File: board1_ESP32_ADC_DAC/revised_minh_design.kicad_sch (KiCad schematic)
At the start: 15 parts, among them J1 Conn_01x03_Male, J2 Conn_01x07_Male, U1 ESP32-DevKit-C, U2 LM7805_TO220, U3 NE5532, U4 CB101

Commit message: -
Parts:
- removed C3: 0.1uF, Capacitor_THT:C_Disc_D6.0mm_W2.5mm_P5.00mm, symbol Device:C
- removed D1: TZX3V6A-TR, Diode_THT:D_DO-35_SOD27_P7.62mm_Horizontal, symbol Device:D_Zener
- removed D2: LED, LED_THT:LED_D3.0mm_Clear, symbol Device:LED
- removed J2: Conn_01x07_Male, Connector_PinSocket_2.54mm:PinSocket_1x07_P2.54mm_Vertical, symbol Connector:Conn_01x07_Male
- removed R1, R2: 10k, Resistor_THT:R_Axial_DIN0309_L9.0mm_D3.2mm_P15.24mm_Horizontal, symbol Device:R
- removed R3: 1K, Resistor_THT:R_Axial_DIN0309_L9.0mm_D3.2mm_P15.24mm_Horizontal, symbol Device:R
- removed R4: 4.7k, Resistor_THT:R_Axial_DIN0309_L9.0mm_D3.2mm_P15.24mm_Horizontal, symbol Device:R
- removed U3: NE5532, Package_DIP:DIP-8_W7.62mm, symbol Amplifier_Operational:NE5532
- removed U4: CB101, Library:CB101, symbol design:CB101
- added C? (x2): 2.2uF, Capacitor_THT:C_Disc_D6.0mm_W2.5mm_P5.00mm, symbol Device:C
- added C?: 1uF, Capacitor_THT:C_Disc_D6.0mm_W2.5mm_P5.00mm, symbol Device:C
- added C?: 1nF, Capacitor_THT:C_Disc_D6.0mm_W2.5mm_P5.00mm, symbol Device:C
- added J?: Conn_01x08_Male, symbol Connector:Conn_01x08_Male
- added R?: 0, symbol Device:R
- added R?: R, symbol Device:R
- added U?: DAC8568IAPW, Package_SO:TSSOP-16-1EP_4.4x5mm_P0.65mm, symbol design:DAC8568IAPW
- added U?: MCP1501-33xSN, Package_SO:SOIC-8_3.9x4.9mm_P1.27mm, symbol Reference_Voltage:MCP1501-33xSN
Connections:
- net +5V: now also C?.1, U?.1 (VDD), U?.3 (~{SHDN})
- net Earth: now also C?.2, C?.2, C?.2, C?.2, U?.14 (GND), U?.2 (GND), U?.4 (GND), U?.5 (GND), U?.6 (GND)
- net +3V3: now reaches U1.20 (3V3)
- net +3V3: now also C?.1, U?.3 (AV_{DD})
- net ~{CS}: now reaches U1.30 (27)
- net ~{CS}: now also U?.2 (~{SYNC})
- net SK: now reaches U1.31 (14)
- net SK: now also U?.16 (SCLK)
- net SO: now reaches U1.34 (13)
- net SO: now also U?.15 (D_{IN})
- net LDAC: now reaches U1.8 (16)
- net LDAC: now also U?.1 (LDAC)
- net ~{CLR}: now reaches U1.9 (17)
- net ~{CLR}: now also U?.9 (~{CLR})
- net DAC_SIG: no longer names the net of U1.28 (25)
- new net: C?.1, R?.2
- new net: R?.2, U?.8 (V_{REF}IN)
- new net +3.3VDAC: C?.1, R?.1, R?.1, U?.7 (OUT), U?.8 (FB)
- new net VoutA: J?.8 (Pin_8), U?.4 (V_{OUT}A)
- new net VoutB: J?.7 (Pin_7), U?.13 (V_{OUT}B)
- new net VoutC: J?.6 (Pin_6), U?.5 (V_{OUT}C)
- new net VoutD: J?.5 (Pin_5), U?.12 (V_{OUT}D)
- new net VoutE: J?.4 (Pin_4), U?.6 (V_{OUT}E)
- new net VoutF: J?.3 (Pin_3), U?.11 (V_{OUT}F)
- new net VoutG: J?.2 (Pin_2), U?.7 (V_{OUT}G)
- new net VoutH: J?.1 (Pin_1), U?.10 (V_{OUT}H)
- no-connect marks 38 -> 28
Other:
- note added: "MOSI"
- note added: "SCLK"
- note removed: "Vout/Vin = 1 + 4.7/10"
- moved on the sheet: C1, C2, J1, U1, U2

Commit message: ADC_DAC
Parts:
- added C11, C4, C5, C6, C7: 0.1uF, Capacitor_SMD:C_0805_2012Metric_Pad1.18x1.45mm_HandSolder, symbol Device:C
- added C3, C8, C9: 10uF, Capacitor_SMD:C_0805_2012Metric_Pad1.18x1.45mm_HandSolder, symbol Device:C
- added J3, J4: Conn_01x08_Male, Connector_PinSocket_2.54mm:PinSocket_1x08_P2.54mm_Vertical, symbol Connector:Conn_01x08_Male
- added R1, R3: 0, Resistor_SMD:R_0805_2012Metric_Pad1.20x1.40mm_HandSolder, symbol Device:R
- added U3: MCP1754S-3302xCB, Package_TO_SOT_SMD:SOT-23, symbol Regulator_Linear:MCP1754S-3302xCB
- added U4: MCP1825S-3.3V, Package_TO_SOT_SMD:SOT-223-3_TabPin2, symbol Regulator_Linear:MCP1825S
- added U6, U7: MCP3464R, Package_SO:TSSOP-20_4.4x6.5mm_P0.65mm, symbol design:MCP3464R
- added X1: ECS-2520MVLC-049-BN-TR, Oscillator:Oscillator_SMD_ECS_2520MV-xxx-xx-4Pin_2.5x2.0mm, symbol Oscillator:ECS-2520MV-xxx-xx
- C1, C2: footprint Capacitor_THT:C_Disc_D6.0mm_W2.5mm_P5.00mm -> Capacitor_SMD:C_0805_2012Metric_Pad1.18x1.45mm_HandSolder
- C10, C12, C13, C14: renamed from C?; footprint Capacitor_THT:C_Disc_D6.0mm_W2.5mm_P5.00mm -> Capacitor_SMD:C_0805_2012Metric_Pad1.18x1.45mm_HandSolder
- J2: renamed from J?; footprint (none) -> Connector_PinSocket_2.54mm:PinSocket_1x08_P2.54mm_Vertical
- R2: renamed from R?; value R -> 50; footprint (none) -> Resistor_SMD:R_0805_2012Metric_Pad1.20x1.40mm_HandSolder
- R4: renamed from R?; footprint (none) -> Resistor_SMD:R_0805_2012Metric_Pad1.20x1.40mm_HandSolder
- gave numbers to parts that had none: 2
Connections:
- net +3.3VDAC: now also U6.4 (REFIN+), U7.4 (REFIN+)
- net +3V3: now also C11.1, C7.1, C9.1, U4.3 (VO), U6.20 (DV_{DD}), U7.20 (DV_{DD}), X1.4 (VDD); no longer U1.20 (3V3)
- net +5V: now also C3.1, C4.1, C5.1, U3.3 (VI), U4.1 (VI)
- net Earth: now also C11.2, C3.2, C5.2, C7.2, C9.2, R1.1, U4.2 (GND), U6.19 (D_{GND}), U7.19 (D_{GND}), X1.2 (GND)
- net SK: now also U6.14 (SCK), U7.14 (SCK)
- net SO: now also U6.16 (SDO), U7.16 (SDO)
- net VoutB: now also J2.1 (Pin_1); no longer J2.7 (Pin_7)
- net VoutC: now also J2.7 (Pin_7); no longer J2.6 (Pin_6)
- net VoutD: now also J2.2 (Pin_2); no longer J2.5 (Pin_5)
- net VoutE: now also J2.6 (Pin_6); no longer J2.4 (Pin_4)
- net VoutG: now also J2.5 (Pin_5); no longer J2.2 (Pin_2)
- net VoutH: now also J2.4 (Pin_4); no longer J2.1 (Pin_1)
- net MDAT: now reaches U1.25 (35)
- net MDAT: now also U6.17 (~{IRQ}/MDAT), U7.17 (~{IRQ}/MDAT)
- net ~{ADC2_CS}: now reaches U1.26 (32)
- net ~{ADC2_CS}: now also U7.13 (~{CS})
- net ~{ADC1_CS}: now reaches U1.27 (33)
- net ~{ADC1_CS}: now also U6.13 (~{CS})
- net SI: now reaches U1.32 (12)
- net SI: now also U6.15 (SDI), U7.15 (SDI)
- net ~{CS} renamed ~{DAC_CS}
- new net: R3.1, X1.3 (OUT)
- new net +3.3VA: C6.1, C8.1, U3.2 (VO), U6.1 (AV_{DD}), U7.1 (AV_{DD})
- new net ADC1_1: J4.1 (Pin_1), U6.5 (CH0)
- new net ADC1_2: J4.2 (Pin_2), U6.6 (CH1)
- new net ADC1_3: J4.3 (Pin_3), U6.7 (CH2)
- new net ADC1_4: J4.4 (Pin_4), U6.8 (CH3)
- new net ADC1_5: J4.5 (Pin_5), U6.9 (CH4)
- new net ADC1_6: J4.6 (Pin_6), U6.10 (CH5)
- new net ADC1_7: J4.7 (Pin_7), U6.11 (CH6)
- new net ADC1_8: J4.8 (Pin_8), U6.12 (CH7)
- new net ADC2_1: J3.1 (Pin_1), U7.5 (CH0)
- new net ADC2_2: J3.2 (Pin_2), U7.6 (CH1)
- new net ADC2_3: J3.3 (Pin_3), U7.7 (CH2)
- new net ADC2_4: J3.4 (Pin_4), U7.8 (CH3)
- new net ADC2_5: J3.5 (Pin_5), U7.9 (CH4)
- new net ADC2_6: J3.6 (Pin_6), U7.10 (CH5)
- new net ADC2_7: J3.7 (Pin_7), U7.11 (CH6)
- new net ADC2_8: J3.8 (Pin_8), U7.12 (CH7)
- new net CLK: R3.2, U6.18 (MLCK), U7.18 (MLCK)
- new net GNDA: C4.2, C6.2, C8.2, R1.2, U3.1 (GND), U6.2 (A_{GND}), U6.3 (REFIN-), U7.2 (A_{GND}), U7.3 (REFIN-)
- no-connect marks 28 -> 26
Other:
- moved on the sheet: C14, J2, R4, U1, U8

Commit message: DAC ground to AGND, new AGND polygon pour
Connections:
- net Earth: no longer U8.14 (GND)
- net GNDA: now also U8.14 (GND)
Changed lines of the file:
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@@
+    (pin "1")
+  )
+  (symbol (lib_id "power:GNDA") (at 220.98 68.58 0) (unit 1)
+    (in_bom yes) (on_board yes)
+    (property "Reference" "#PWR?" (id 0) (at 220.98 74.93 0)
+      (effects (font (size 1.27 1.27)) hide)
+    )
+    (property "Value" "GNDA" (id 1) (at 217.17 69.85 0))
+    (property "Footprint" "" (id 2) (at 220.98 68.58 0)
+      (effects (font (size 1.27 1.27)) hide)
+    )
+    (property "Datasheet" "" (id 3) (at 220.98 68.58 0)
+      (effects (font (size 1.27 1.27)) hide)
+    )
     (pin "1")
   )
@@
     (pin "1")
   )
-  (symbol (lib_id "power:Earth") (at 220.98 68.58 0) (unit 1)
-    (in_bom yes) (on_board yes) (fields_autoplaced)
-    (property "Reference" "#PWR040" (id 0) (at 220.98 74.93 0)
-      (effects (font (size 1.27 1.27)) hide)
-    )
-    (property "Value" "Earth" (id 1) (at 220.98 72.39 0)
-      (effects (font (size 1.27 1.27)) hide)
-    )
-    (property "Footprint" "" (id 2) (at 220.98 68.58 0)
-      (effects (font (size 1.27 1.27)) hide)
-    )
-    (property "Datasheet" "~" (id 3) (at 220.98 68.58 0)
-      (effects (font (size 1.27 1.27)) hide)
-    )
-    (pin "1")
-  )
   (symbol (lib_id "Device:C") (at 87.63 33.02 0) (unit 1)
     (in_bom yes) (on_board yes) (fields_autoplaced)
@@
       (reference "#PWR039") (unit 1) (value "Earth") (footprint "")
     )
-    (path "/ded4a434-8dc3-4ae9-9c86-aa80321c8438"
-      (reference "#PWR040") (unit 1) (value "Earth") (footprint "")
-    )
     (path "/a693dd2a-10f5-49e8-8ed2-7ff749236d48"
       (reference "#PWR041") (unit 1) (value "+3.3V") (footprint "")
@@
       (reference "#PWR047") (unit 1) (value "+3.3V") (footprint "")
     )
+    (path "/1608183c-7910-43a9-a0f7-77336bb08a03"
+      (reference "#PWR?") (unit 1) (value "GNDA") (footprint "")
+    )
     (path "/f1973fc8-15b6-4c53-87c0-78a3b2cf3358"

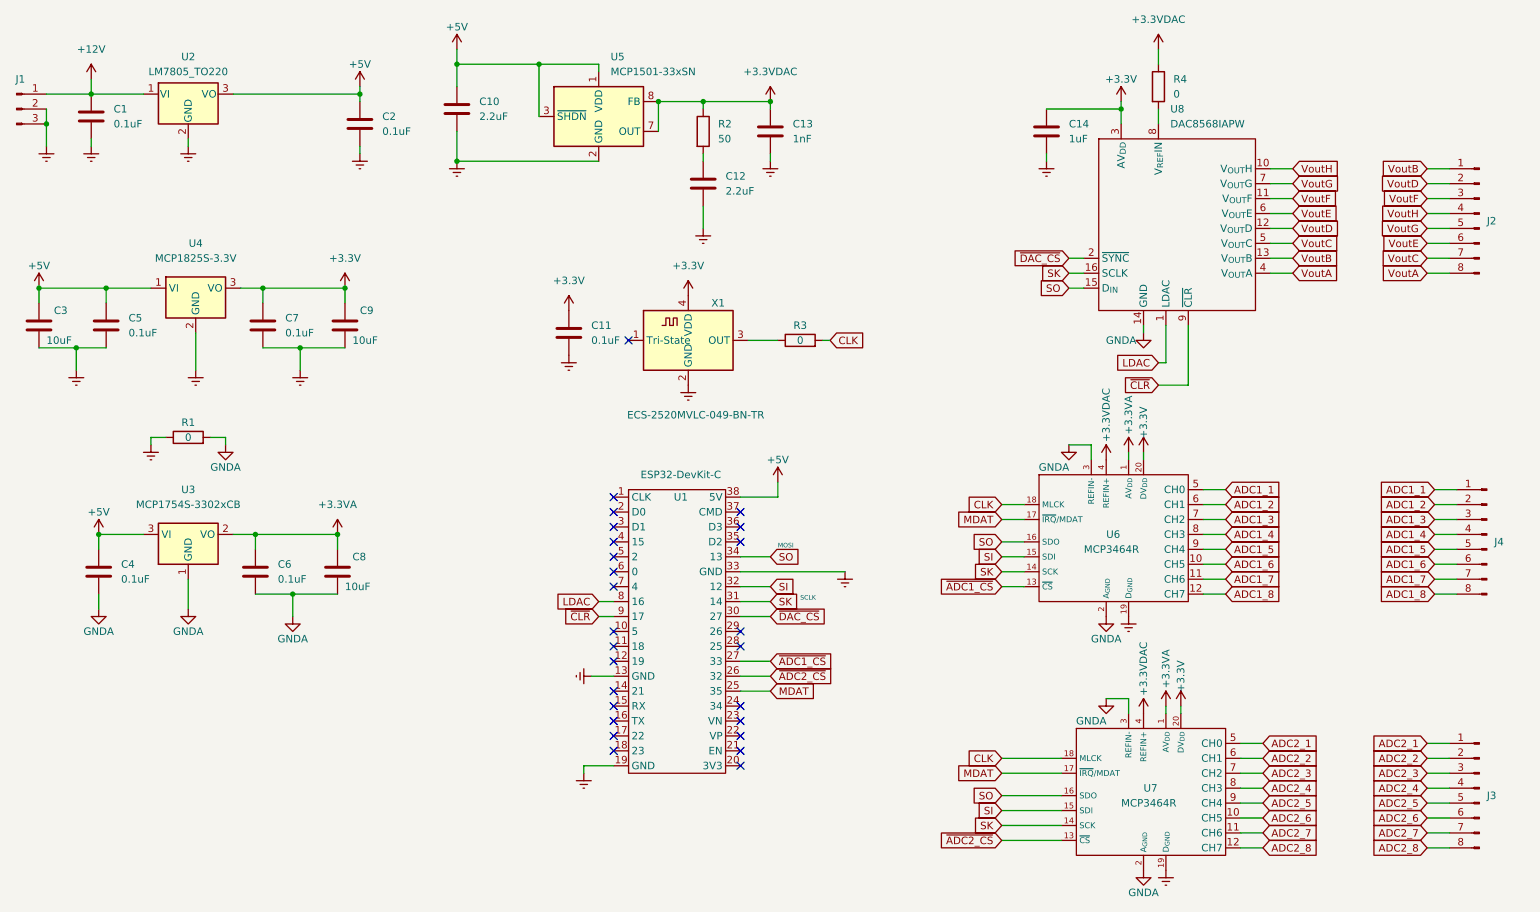
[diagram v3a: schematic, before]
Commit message: Fab ready version with joined ground plane, extra caps for ADCs
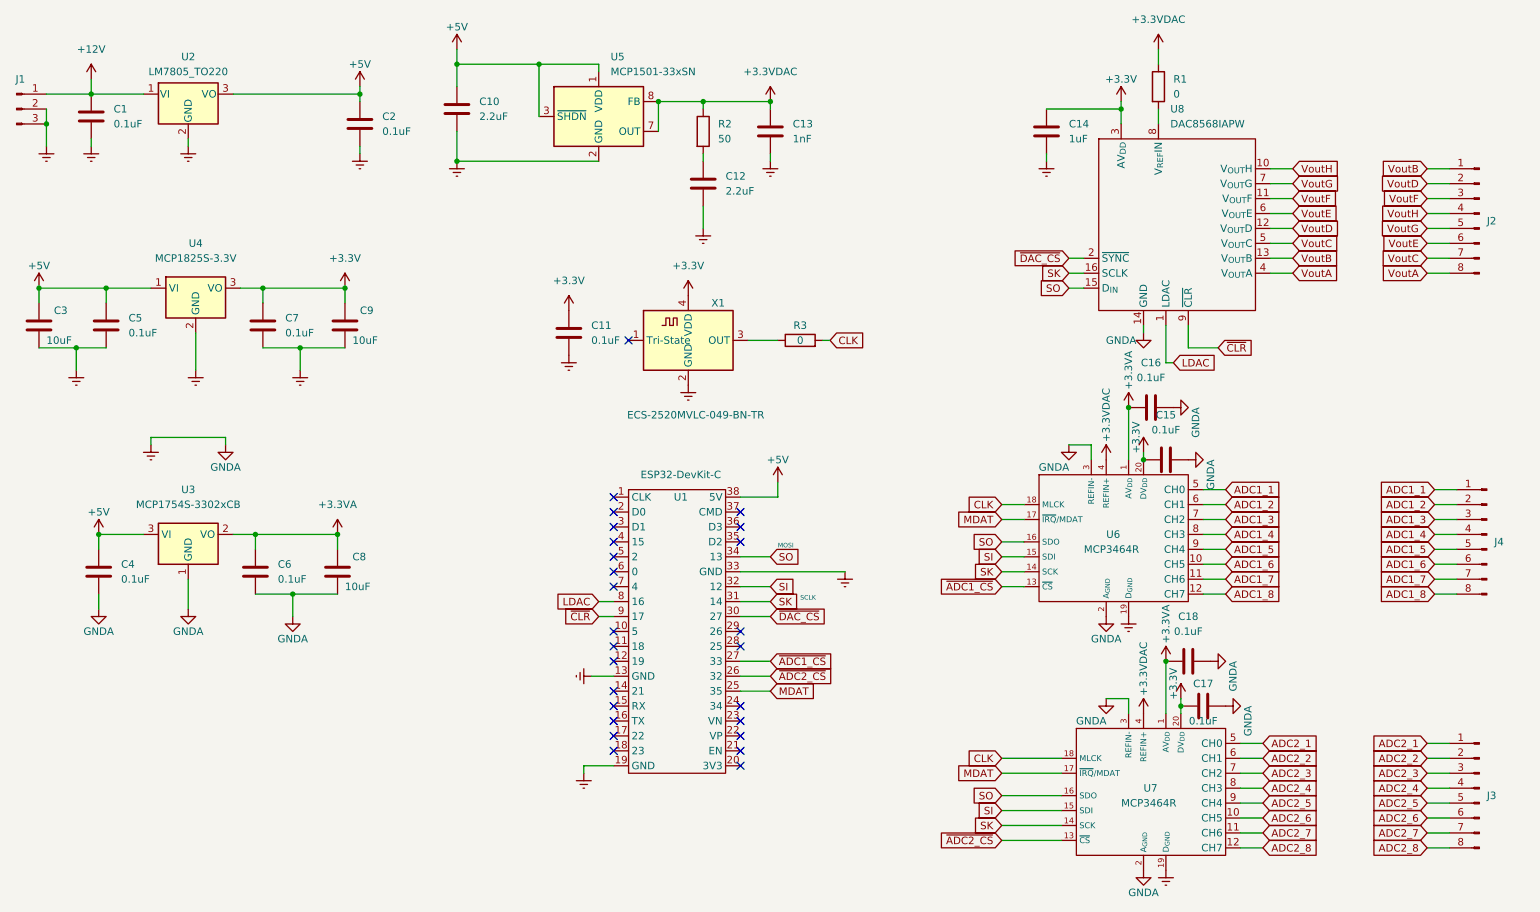
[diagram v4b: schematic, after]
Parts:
- removed R1: 0, Resistor_SMD:R_0805_2012Metric_Pad1.20x1.40mm_HandSolder, symbol Device:R
- added C15, C16, C17, C18: 0.1uF, Capacitor_SMD:C_0805_2012Metric_Pad1.18x1.45mm_HandSolder, symbol Device:C
- renumbered R4 to R1
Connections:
- net GNDA is gone; now on net Earth: C4.2, C6.2, C8.2, U3.1 (GND), U6.2 (A_{GND}), U6.3 (REFIN-), U7.2 (A_{GND}), U7.3 (REFIN-), U8.14 (GND)
- net +3.3VA: now also C16.1, C18.1
- net +3V3: now also C15.1, C17.1
- net Earth: now also C15.2, C16.2, C17.2, C18.2

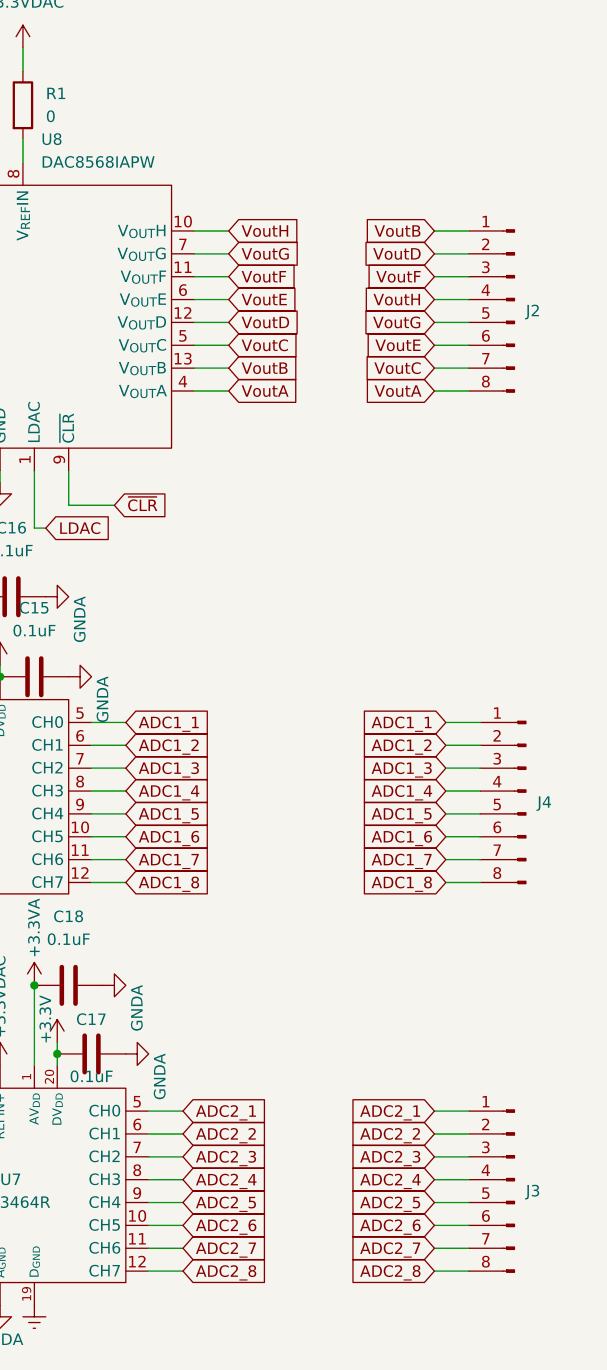
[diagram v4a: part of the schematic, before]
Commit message: JLCPB Submission. Name added, connectors changed to double layer
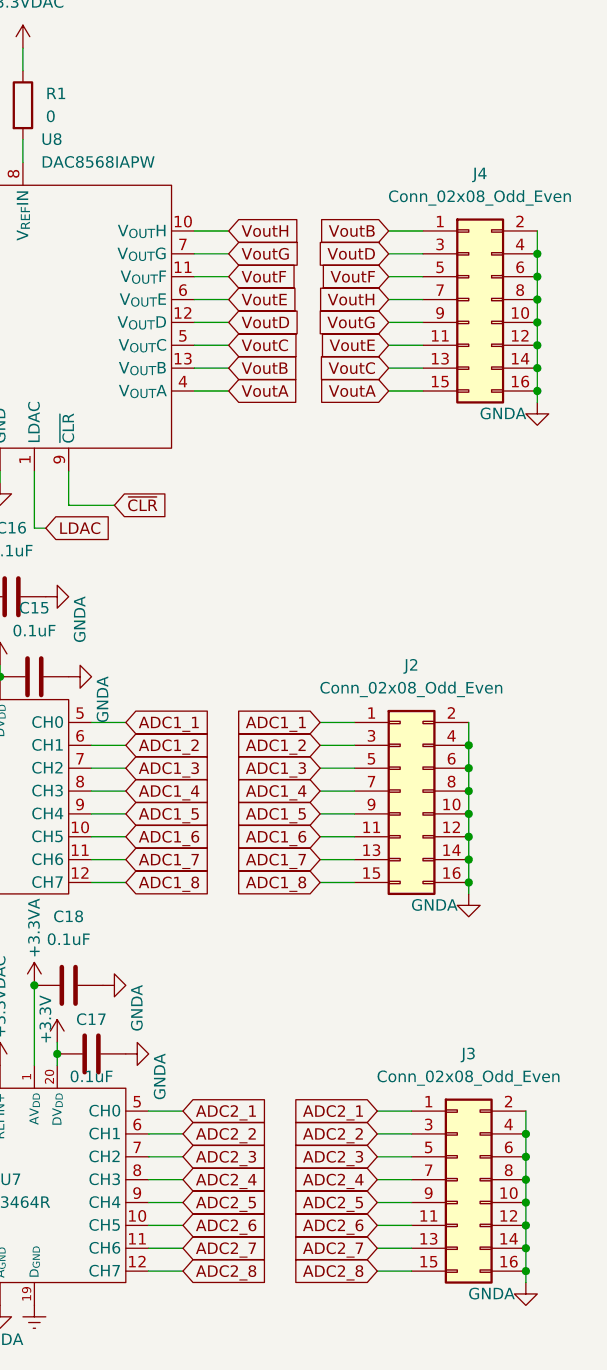
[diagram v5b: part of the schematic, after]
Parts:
- removed J2, J3, J4: Conn_01x08_Male, Connector_PinSocket_2.54mm:PinSocket_1x08_P2.54mm_Vertical, symbol Connector:Conn_01x08_Male
- added J2, J3, J4: Conn_02x08_Odd_Even, Connector_PinSocket_2.54mm:PinSocket_2x08_P2.54mm_Vertical, symbol Connector_Generic:Conn_02x08_Odd_Even
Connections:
- net ADC1_1: now also J2.1 (Pin_1)
- net ADC1_2: now also J2.3 (Pin_3)
- net ADC1_3: now also J2.5 (Pin_5)
- net ADC1_4: now also J2.7 (Pin_7)
- net ADC1_5: now also J2.9 (Pin_9)
- net ADC1_6: now also J2.11 (Pin_11)
- net ADC1_7: now also J2.13 (Pin_13)
- net ADC1_8: now also J2.15 (Pin_15)
- net ADC2_1: now also J3.1 (Pin_1)
- net ADC2_2: now also J3.3 (Pin_3)
- net ADC2_3: now also J3.5 (Pin_5)
- net ADC2_4: now also J3.7 (Pin_7)
- net ADC2_5: now also J3.9 (Pin_9)
- net ADC2_6: now also J3.11 (Pin_11)
- net ADC2_7: now also J3.13 (Pin_13)
- net ADC2_8: now also J3.15 (Pin_15)
- net Earth: now also J2.10 (Pin_10), J2.12 (Pin_12), J2.14 (Pin_14), J2.16 (Pin_16), J2.2 (Pin_2), J2.4 (Pin_4), J2.6 (Pin_6), J2.8 (Pin_8), J3.10 (Pin_10), J3.12 (Pin_12), J3.14 (Pin_14), J3.16 (Pin_16), J3.2 (Pin_2), J3.4 (Pin_4), J3.6 (Pin_6), J3.8 (Pin_8), J4.10 (Pin_10), J4.12 (Pin_12), J4.14 (Pin_14), J4.16 (Pin_16), J4.2 (Pin_2), J4.4 (Pin_4), J4.6 (Pin_6), J4.8 (Pin_8)
- net VoutA: now also J4.15 (Pin_15)
- net VoutB: now also J4.1 (Pin_1)
- net VoutC: now also J4.13 (Pin_13)
- net VoutD: now also J4.3 (Pin_3)
- net VoutE: now also J4.11 (Pin_11)
- net VoutF: now also J4.5 (Pin_5)
- net VoutG: now also J4.9 (Pin_9)
- net VoutH: now also J4.7 (Pin_7)
